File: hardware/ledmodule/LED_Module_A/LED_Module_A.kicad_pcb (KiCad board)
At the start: 2 copper layers, 214.6 x 70.5 mm, 148 parts, among them J1 Connector Header Surface Moun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, U1 DS18B20U+

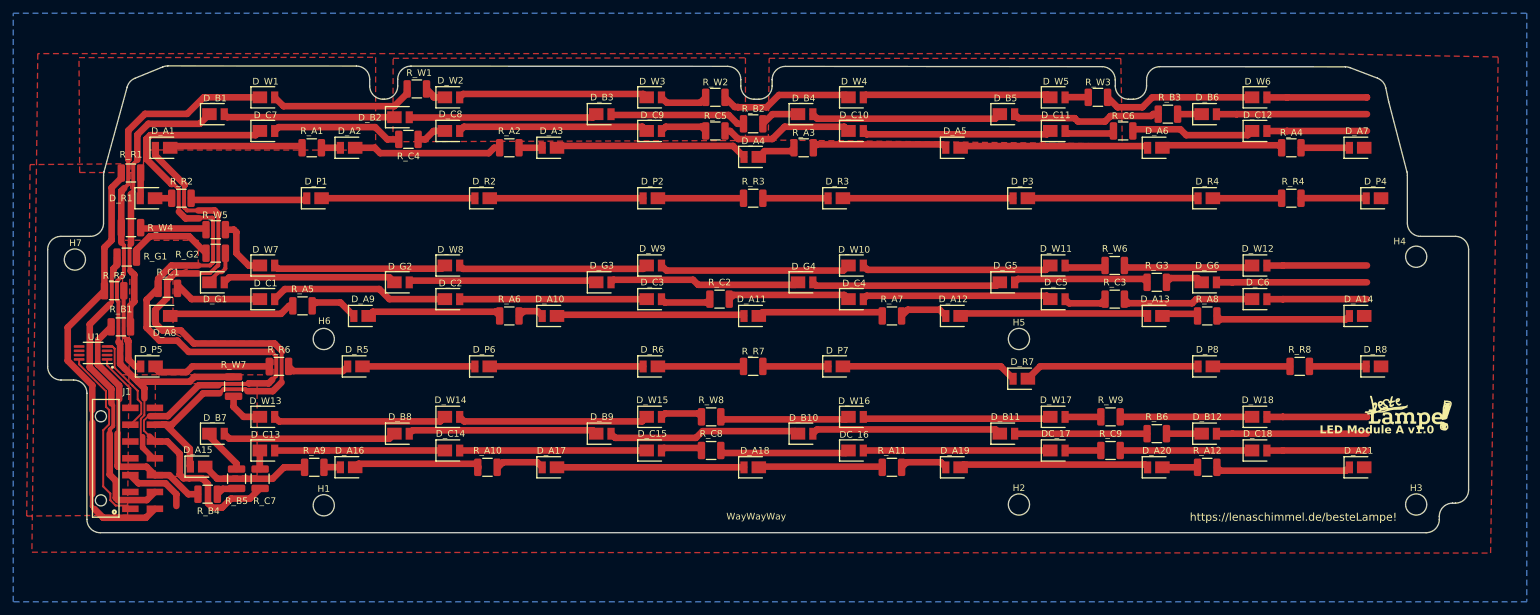
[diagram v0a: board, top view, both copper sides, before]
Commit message: Added test points and a lot more silkscreen.
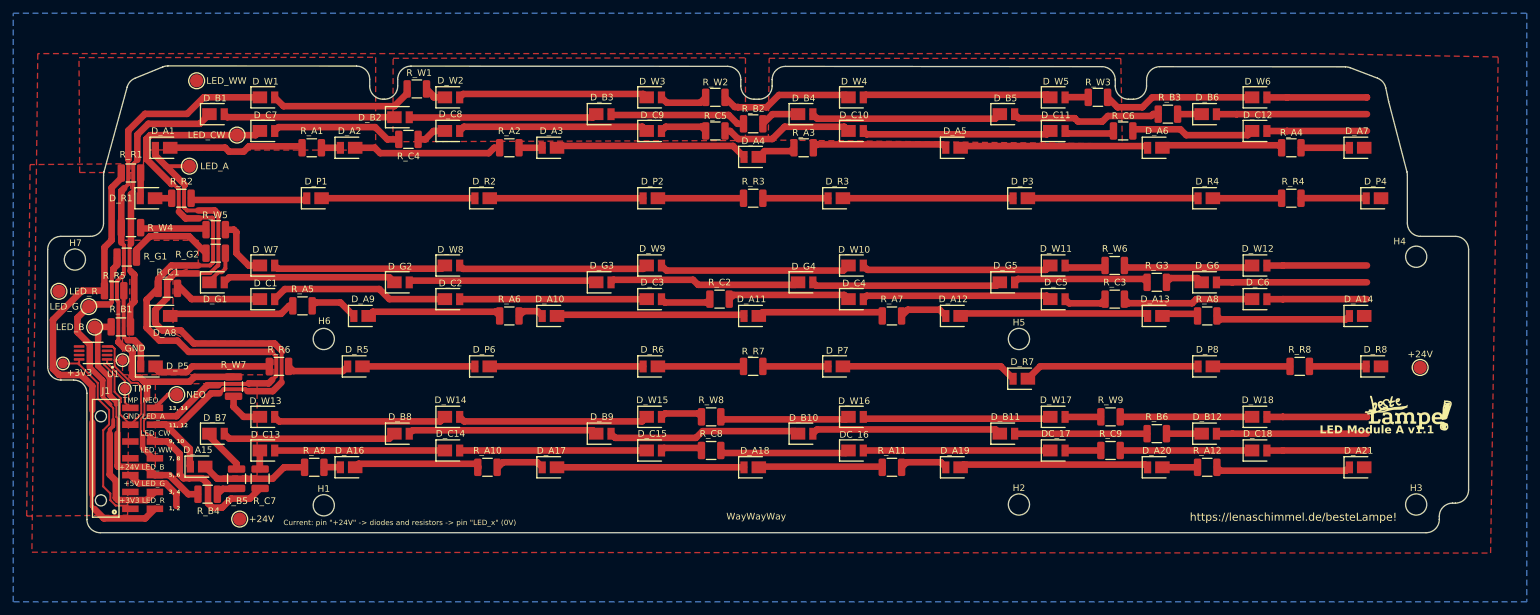
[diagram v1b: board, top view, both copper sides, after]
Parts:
- added +24V: TestPoint_Pad_D2.0mm, TestPoint:TestPoint_Pad_D2.0mm, F.Cu at (250.6, 104.3)
- added +24V: TestPoint_Pad_D2.0mm, TestPoint:TestPoint_Pad_D2.0mm, F.Cu at (72.3, 127.2)
- added +3V3: TestPoint_Pad_D1.5mm, TestPoint:TestPoint_Pad_D1.5mm, F.Cu at (45.6, 103.7)
- added GND: TestPoint_Pad_D1.5mm, TestPoint:TestPoint_Pad_D1.5mm, F.Cu at (54.6, 103.2)
- added LED_A: TestPoint_Pad_D2.0mm, TestPoint:TestPoint_Pad_D2.0mm, F.Cu at (64.7, 73.9)
- added LED_B: TestPoint_Pad_D2.0mm, TestPoint:TestPoint_Pad_D2.0mm, F.Cu at (50.4, 98.2)
- added LED_CW: TestPoint_Pad_D2.0mm, TestPoint:TestPoint_Pad_D2.0mm, F.Cu at (71.9, 69.2)
- added LED_G: TestPoint_Pad_D2.0mm, TestPoint:TestPoint_Pad_D2.0mm, F.Cu at (49.5, 95.1)
- added LED_R: TestPoint_Pad_D2.0mm, TestPoint:TestPoint_Pad_D2.0mm, F.Cu at (45.0, 92.8)
- added LED_WW: TestPoint_Pad_D2.0mm, TestPoint:TestPoint_Pad_D2.0mm, F.Cu at (65.8, 61.0)
- added NEO: TestPoint_Pad_D2.0mm, TestPoint:TestPoint_Pad_D2.0mm, F.Cu at (62.8, 108.4)
- added TMP: TestPoint_Pad_D1.5mm, TestPoint:TestPoint_Pad_D1.5mm, F.Cu at (55.0, 107.5)
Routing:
- net GND: track 15.6 -> 28.3 mm
- net /LED_R: track 66.1 -> 72.0 mm
- net /NEO: track 0.00 -> 4.14 mm
- net /LED_A: track 96.0 -> 99.6 mm
- net /LED_G: track 46.7 -> 49.9 mm
- net +3V3: track 27.5 -> 29.8 mm
- net /LED_B: track 37.9 -> 39.2 mm
- net /LED_WW: track 92.3 -> 93.1 mm
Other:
- board text added: "+24V LED_B"
- board text added: "+3V3 LED_R"
- board text added: "+5V LED_G"
- board text added: "1, 2"
- board text added: "11, 12"
- board text added: "13, 14"
- board text added: "3, 4"
- board text added: "5, 6"
- board text added: "7, 8"
- board text added: "9, 10"
- board text added: "Current: pin {dblquote}+24V{dblquote} -> diodes and resistors -> pin {dblquote}LED_x{dblquote} (0V)"
- board text added: "GND LED_A"
- board text added: "LED Module A v1.1"
- board text added: "LED_CW"
- board text added: "LED_WW"
- board text added: "TMP NEO"
- board text removed: "LED Module A v1.0"
